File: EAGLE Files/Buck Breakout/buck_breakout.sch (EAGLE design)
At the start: 14 parts

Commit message: Added linear reg to power board. Layout ver 1.
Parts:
- added C7: 1000pF, chips:CAP0603-CAP
- added C8: 1uF, chips:CAP0603-CAP
- added LED2: (no value), chips:LED0603
- added R5, R6: 1M, chips:RESISTOR0402-S
- added R7: 330, chips:RESISTOR0402-S
- added U$2: MCP1725, intelliDesk:MCP1725
- C3: device chips:CAP1206 -> chips:CAP0603-CAP
- JP1: device SparkFun-Connectors:M03PTH -> SparkFun-Connectors:M04PTH
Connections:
- removed net VOUT: C4.1, C5.1, C6.1, JP1.3, L1.2, R2.2, R4.2, U$1.BD
- new net 3.3V: C8.1, JP1.4, R5.2, R7.1, U$2.VOUT
- new net 3.6V: C4.1, C5.1, C6.1, JP1.3, L1.2, R2.2, R4.2, U$1.BD, U$2.SHDN#, U$2.VIN
- new net N$1: LED2.A, R7.2, U$2.PWRGD
- new net N$5: C7.1, U$2.CDELAY
- new net N$6: R5.1, R6.2, U$2.ADJ
- net GND: now also C7.2, C8.2, LED2.C, R6.1, U$2.GND

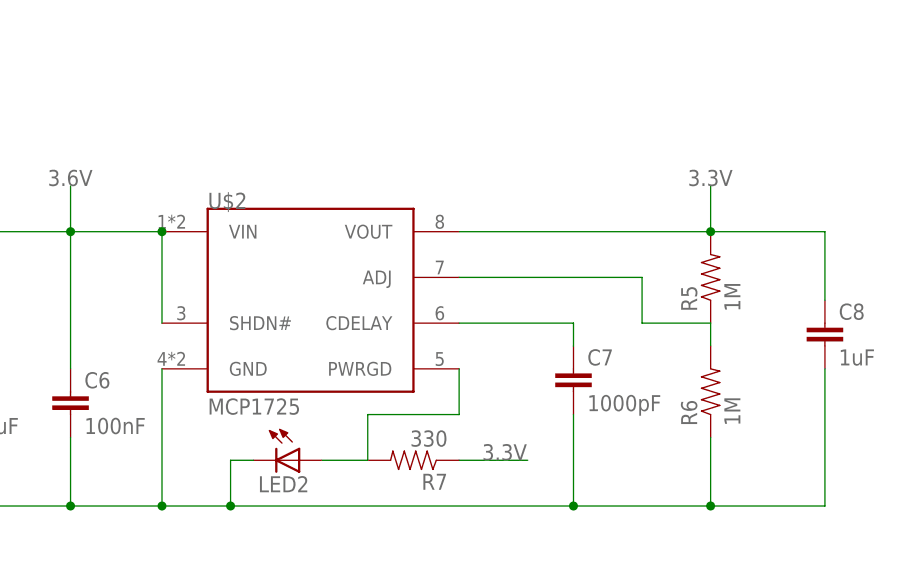
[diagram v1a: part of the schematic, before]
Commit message: Rerouted for nicer layout on linear supply
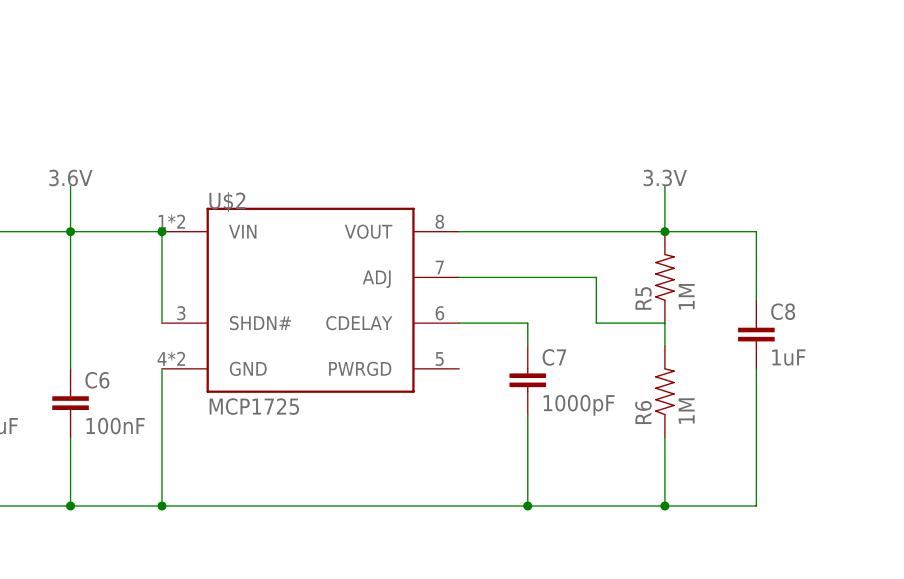
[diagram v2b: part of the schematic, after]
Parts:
- removed LED2: (no value), chips:LED0603
- removed R7: 330, chips:RESISTOR0402-S
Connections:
- removed net N$1: LED2.A, R7.2, U$2.PWRGD
- net 3.3V: no longer R7.1
- net GND: no longer LED2.C
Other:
- moved on the sheet: C7, C8, R5, R6
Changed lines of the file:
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@@
 <part name="R5" library="chips" deviceset="RESISTOR" device="0402-S" value="1M"/>
 <part name="R6" library="chips" deviceset="RESISTOR" device="0402-S" value="1M"/>
-<part name="R7" library="chips" deviceset="RESISTOR" device="0402-S" value="330"/>
-<part name="LED2" library="chips" deviceset="LED" device="0603"/>
 <part name="C7" library="chips" deviceset="CAP" device="0603-CAP" value="1000pF"/>
 <part name="C8" library="chips" deviceset="CAP" device="0603-CAP" value="1uF"/>
@@
 <instance part="GND2" gate="1" x="119.38" y="91.44"/>
 <instance part="U$2" gate="G$1" x="154.94" y="50.8"/>
-<instance part="R5" gate="G$1" x="198.12" y="53.34" rot="R90"/>
-<instance part="R6" gate="G$1" x="198.12" y="40.64" rot="R90"/>
-<instance part="R7" gate="G$1" x="165.1" y="33.02" rot="R180"/>
-<instance part="LED2" gate="G$1" x="152.4" y="33.02" rot="R270"/>
-<instance part="C7" gate="G$1" x="182.88" y="40.64"/>
-<instance part="C8" gate="G$1" x="210.82" y="45.72"/>
+<instance part="R5" gate="G$1" x="193.04" y="53.34" rot="R90"/>
+<instance part="R6" gate="G$1" x="193.04" y="40.64" rot="R90"/>
+<instance part="C7" gate="G$1" x="177.8" y="40.64"/>
+<instance part="C8" gate="G$1" x="203.2" y="45.72"/>
 </instances>
 <busses>
@@
 <pinref part="C7" gate="G$1" pin="2"/>
 <wire x1="127" y1="27.94" x2="114.3" y2="27.94" width="0.1524" layer="91"/>
-<wire x1="137.16" y1="27.94" x2="144.78" y2="27.94" width="0.1524" layer="91"/>
-<wire x1="144.78" y1="27.94" x2="182.88" y2="27.94" width="0.1524" layer="91"/>
-<wire x1="182.88" y1="27.94" x2="182.88" y2="38.1" width="0.1524" layer="91"/>
-<pinref part="LED2" gate="G$1" pin="C"/>
-<wire x1="147.32" y1="33.02" x2="144.78" y2="33.02" width="0.1524" layer="91"/>
-<wire x1="144.78" y1="33.02" x2="144.78" y2="27.94" width="0.1524" layer="91"/>
+<wire x1="137.16" y1="27.94" x2="177.8" y2="27.94" width="0.1524" layer="91"/>
+<wire x1="177.8" y1="27.94" x2="177.8" y2="38.1" width="0.1524" layer="91"/>
 <junction x="137.16" y="27.94"/>
-<junction x="144.78" y="27.94"/>
 <pinref part="R6" gate="G$1" pin="1"/>
-<wire x1="182.88" y1="27.94" x2="198.12" y2="27.94" width="0.1524" layer="91"/>
-<wire x1="198.12" y1="27.94" x2="198.12" y2="35.56" width="0.1524" layer="91"/>
-<junction x="182.88" y="27.94"/>
+<wire x1="177.8" y1="27.94" x2="193.04" y2="27.94" width="0.1524" layer="91"/>
+<wire x1="193.04" y1="27.94" x2="193.04" y2="35.56" width="0.1524" layer="91"/>
+<junction x="177.8" y="27.94"/>
 <pinref part="C8" gate="G$1" pin="2"/>
-<wire x1="210.82" y1="43.18" x2="210.82" y2="27.94" width="0.1524" layer="91"/>
-<wire x1="210.82" y1="27.94" x2="198.12" y2="27.94" width="0.1524" layer="91"/>
-<junction x="198.12" y="27.94"/>
+<wire x1="203.2" y1="43.18" x2="203.2" y2="27.94" width="0.1524" layer="91"/>
+<wire x1="203.2" y1="27.94" x2="193.04" y2="27.94" width="0.1524" layer="91"/>
+<junction x="193.04" y="27.94"/>
 <pinref part="C6" gate="G$1" pin="2"/>
 <wire x1="127" y1="35.56" x2="127" y2="27.94" width="0.1524" layer="91"/>
@@
 <pinref part="U$2" gate="G$1" pin="CDELAY"/>
 <pinref part="C7" gate="G$1" pin="1"/>
-<wire x1="170.18" y1="48.26" x2="182.88" y2="48.26" width="0.1524" layer="91"/>
-<wire x1="182.88" y1="48.26" x2="182.88" y2="45.72" width="0.1524" layer="91"/>
+<wire x1="170.18" y1="48.26" x2="177.8" y2="48.26" width="0.1524" layer="91"/>
+<wire x1="177.8" y1="48.26" x2="177.8" y2="45.72" width="0.1524" layer="91"/>
 </segment>
 </net>
@@
 <pinref part="R6" gate="G$1" pin="2"/>
 <pinref part="R5" gate="G$1" pin="1"/>
-<wire x1="198.12" y1="45.72" x2="198.12" y2="48.26" width="0.1524" layer="91"/>
-<wire x1="198.12" y1="48.26" x2="190.5" y2="48.26" width="0.1524" layer="91"/>
-<wire x1="190.5" y1="48.26" x2="190.5" y2="53.34" width="0.1524" layer="91"/>
+<wire x1="193.04" y1="45.72" x2="193.04" y2="48.26" width="0.1524" layer="91"/>
+<wire x1="193.04" y1="48.26" x2="185.42" y2="48.26" width="0.1524" layer="91"/>
+<wire x1="185.42" y1="48.26" x2="185.42" y2="53.34" width="0.1524" layer="91"/>
 <pinref part="U$2" gate="G$1" pin="ADJ"/>
-<wire x1="190.5" y1="53.34" x2="170.18" y2="53.34" width="0.1524" layer="91"/>
-</segment>
-</net>
-<net name="N$1" class="0">
-<segment>
-<pinref part="U$2" gate="G$1" pin="PWRGD"/>
-<wire x1="170.18" y1="43.18" x2="170.18" y2="38.1" width="0.1524" layer="91"/>
-<pinref part="R7" gate="G$1" pin="2"/>
-<wire x1="170.18" y1="38.1" x2="160.02" y2="38.1" width="0.1524" layer="91"/>
-<wire x1="160.02" y1="38.1" x2="160.02" y2="33.02" width="0.1524" layer="91"/>
-<pinref part="LED2" gate="G$1" pin="A"/>
-<wire x1="160.02" y1="33.02" x2="154.94" y2="33.02" width="0.1524" layer="91"/>
+<wire x1="185.42" y1="53.34" x2="170.18" y2="53.34" width="0.1524" layer="91"/>
 </segment>
 </net>
 <net name="3.3V" class="0">
 <segment>
-<pinref part="R7" gate="G$1" pin="1"/>
-<wire x1="170.18" y1="33.02" x2="177.8" y2="33.02" width="0.1524" layer="91"/>
-<label x="172.72" y="33.02" size="1.778" layer="95"/>
-</segment>
-<segment>
 <pinref part="U$2" gate="G$1" pin="VOUT"/>
-<wire x1="170.18" y1="58.42" x2="198.12" y2="58.42" width="0.1524" layer="91"/>
+<wire x1="170.18" y1="58.42" x2="193.04" y2="58.42" width="0.1524" layer="91"/>
 <pinref part="R5" gate="G$1" pin="2"/>
-<wire x1="198.12" y1="58.42" x2="210.82" y2="58.42" width="0.1524" layer="91"/>
-<junction x="198.12" y="58.42"/>
+<wire x1="193.04" y1="58.42" x2="203.2" y2="58.42" width="0.1524" layer="91"/>
+<junction x="193.04" y="58.42"/>
 <pinref part="C8" gate="G$1" pin="1"/>
-<wire x1="210.82" y1="58.42" x2="210.82" y2="50.8" width="0.1524" layer="91"/>
-<wire x1="198.12" y1="58.42" x2="198.12" y2="63.5" width="0.1524" layer="91"/>
-<label x="195.58" y="63.5" size="1.778" layer="95"/>
-</segment>
-<segment>
+<wire x1="203.2" y1="58.42" x2="203.2" y2="50.8" width="0.1524" layer="91"/>
+<wire x1="193.04" y1="58.42" x2="193.04" y2="63.5" width="0.1524" layer="91"/>
+<label x="190.5" y="63.5" size="1.778" layer="95"/>
+</segment>
+<segment>

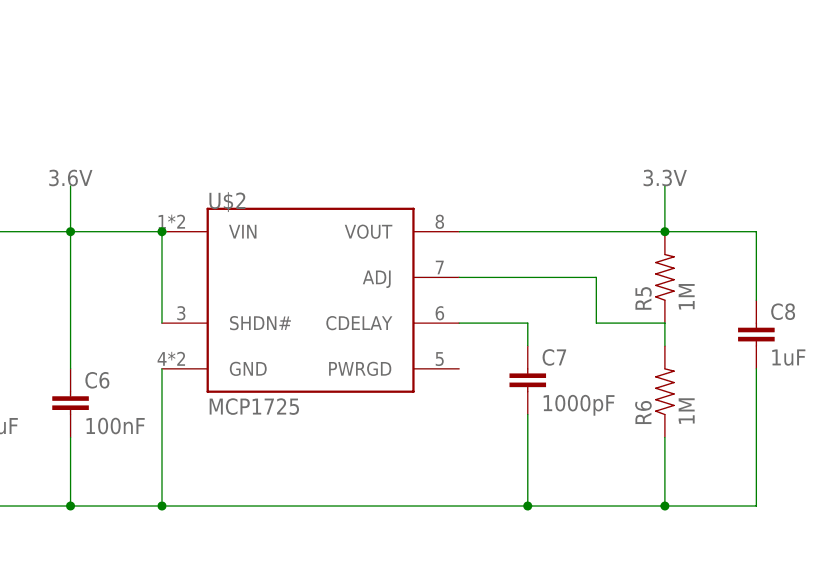
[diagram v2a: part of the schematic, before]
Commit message: fixed via size and removed most silkscreen on power breakout pcb
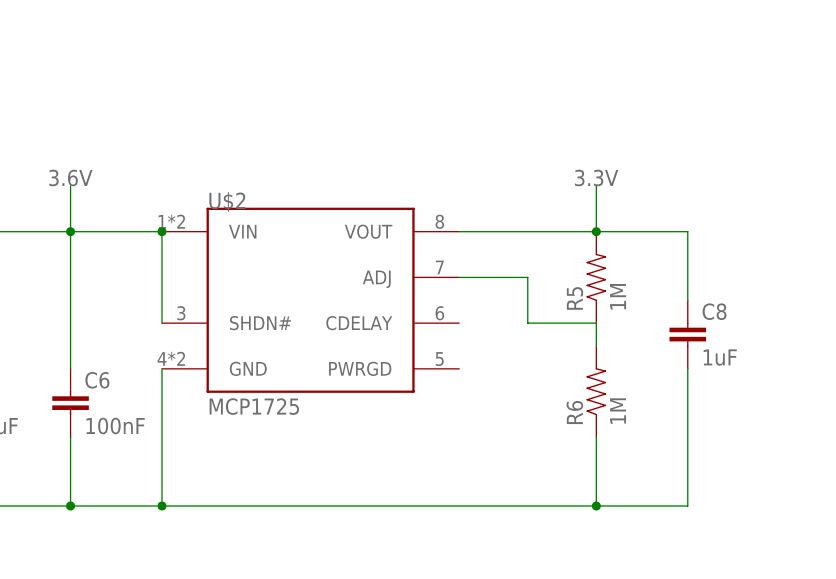
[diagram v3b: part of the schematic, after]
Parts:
- removed C7: 1000pF, chips:CAP0603-CAP
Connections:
- removed net N$5: C7.1, U$2.CDELAY
- net GND: no longer C7.2
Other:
- moved on the sheet: C8, R5, R6
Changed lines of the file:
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@@
 <part name="R5" library="chips" deviceset="RESISTOR" device="0402-S" value="1M"/>
 <part name="R6" library="chips" deviceset="RESISTOR" device="0402-S" value="1M"/>
-<part name="C7" library="chips" deviceset="CAP" device="0603-CAP" value="1000pF"/>
 <part name="C8" library="chips" deviceset="CAP" device="0603-CAP" value="1uF"/>
 </parts>
@@
 <instance part="GND2" gate="1" x="119.38" y="91.44"/>
 <instance part="U$2" gate="G$1" x="154.94" y="50.8"/>
-<instance part="R5" gate="G$1" x="193.04" y="53.34" rot="R90"/>
-<instance part="R6" gate="G$1" x="193.04" y="40.64" rot="R90"/>
-<instance part="C7" gate="G$1" x="177.8" y="40.64"/>
-<instance part="C8" gate="G$1" x="203.2" y="45.72"/>
+<instance part="R5" gate="G$1" x="185.42" y="53.34" rot="R90"/>
+<instance part="R6" gate="G$1" x="185.42" y="40.64" rot="R90"/>
+<instance part="C8" gate="G$1" x="195.58" y="45.72"/>
 </instances>
 <busses>
@@
 <wire x1="137.16" y1="27.94" x2="127" y2="27.94" width="0.1524" layer="91"/>
 <junction x="114.3" y="27.94"/>
-<pinref part="C7" gate="G$1" pin="2"/>
 <wire x1="127" y1="27.94" x2="114.3" y2="27.94" width="0.1524" layer="91"/>
-<wire x1="137.16" y1="27.94" x2="177.8" y2="27.94" width="0.1524" layer="91"/>
-<wire x1="177.8" y1="27.94" x2="177.8" y2="38.1" width="0.1524" layer="91"/>
+<wire x1="137.16" y1="27.94" x2="185.42" y2="27.94" width="0.1524" layer="91"/>
 <junction x="137.16" y="27.94"/>
 <pinref part="R6" gate="G$1" pin="1"/>
-<wire x1="177.8" y1="27.94" x2="193.04" y2="27.94" width="0.1524" layer="91"/>
-<wire x1="193.04" y1="27.94" x2="193.04" y2="35.56" width="0.1524" layer="91"/>
-<junction x="177.8" y="27.94"/>
+<wire x1="185.42" y1="27.94" x2="185.42" y2="35.56" width="0.1524" layer="91"/>
 <pinref part="C8" gate="G$1" pin="2"/>
-<wire x1="203.2" y1="43.18" x2="203.2" y2="27.94" width="0.1524" layer="91"/>
-<wire x1="203.2" y1="27.94" x2="193.04" y2="27.94" width="0.1524" layer="91"/>
-<junction x="193.04" y="27.94"/>
+<wire x1="195.58" y1="43.18" x2="195.58" y2="27.94" width="0.1524" layer="91"/>
+<wire x1="195.58" y1="27.94" x2="185.42" y2="27.94" width="0.1524" layer="91"/>
+<junction x="185.42" y="27.94"/>
 <pinref part="C6" gate="G$1" pin="2"/>
 <wire x1="127" y1="35.56" x2="127" y2="27.94" width="0.1524" layer="91"/>
@@
 </segment>
 </net>
-<net name="N$5" class="0">
-<segment>
-<pinref part="U$2" gate="G$1" pin="CDELAY"/>
-<pinref part="C7" gate="G$1" pin="1"/>
-<wire x1="170.18" y1="48.26" x2="177.8" y2="48.26" width="0.1524" layer="91"/>
-<wire x1="177.8" y1="48.26" x2="177.8" y2="45.72" width="0.1524" layer="91"/>
-</segment>
-</net>
 <net name="N$6" class="0">
 <segment>
 <pinref part="R6" gate="G$1" pin="2"/>
 <pinref part="R5" gate="G$1" pin="1"/>
-<wire x1="193.04" y1="45.72" x2="193.04" y2="48.26" width="0.1524" layer="91"/>
-<wire x1="193.04" y1="48.26" x2="185.42" y2="48.26" width="0.1524" layer="91"/>
-<wire x1="185.42" y1="48.26" x2="185.42" y2="53.34" width="0.1524" layer="91"/>
+<wire x1="185.42" y1="45.72" x2="185.42" y2="48.26" width="0.1524" layer="91"/>
+<wire x1="185.42" y1="48.26" x2="177.8" y2="48.26" width="0.1524" layer="91"/>
+<wire x1="177.8" y1="48.26" x2="177.8" y2="53.34" width="0.1524" layer="91"/>
 <pinref part="U$2" gate="G$1" pin="ADJ"/>
-<wire x1="185.42" y1="53.34" x2="170.18" y2="53.34" width="0.1524" layer="91"/>
+<wire x1="177.8" y1="53.34" x2="170.18" y2="53.34" width="0.1524" layer="91"/>
 </segment>
 </net>
@@
 <segment>
 <pinref part="U$2" gate="G$1" pin="VOUT"/>
-<wire x1="170.18" y1="58.42" x2="193.04" y2="58.42" width="0.1524" layer="91"/>
+<wire x1="170.18" y1="58.42" x2="185.42" y2="58.42" width="0.1524" layer="91"/>
 <pinref part="R5" gate="G$1" pin="2"/>
-<wire x1="193.04" y1="58.42" x2="203.2" y2="58.42" width="0.1524" layer="91"/>
-<junction x="193.04" y="58.42"/>
+<wire x1="185.42" y1="58.42" x2="195.58" y2="58.42" width="0.1524" layer="91"/>
+<junction x="185.42" y="58.42"/>
 <pinref part="C8" gate="G$1" pin="1"/>
-<wire x1="203.2" y1="58.42" x2="203.2" y2="50.8" width="0.1524" layer="91"/>
-<wire x1="193.04" y1="58.42" x2="193.04" y2="63.5" width="0.1524" layer="91"/>
-<label x="190.5" y="63.5" size="1.778" layer="95"/>
-</segment>
-<segment>
+<wire x1="195.58" y1="58.42" x2="195.58" y2="50.8" width="0.1524" layer="91"/>
+<wire x1="185.42" y1="58.42" x2="185.42" y2="63.5" width="0.1524" layer="91"/>
+<label x="182.88" y="63.5" size="1.778" layer="95"/>
+</segment>
+<segment>

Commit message: Added OLED breakout board. (not yet designed) Added linear regulator datasheet. Updated parts library.
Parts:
- R5: value 1M -> 1.1M
- R6: value 1M -> 160k
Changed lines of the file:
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@@
 <part name="GND2" library="supply1" deviceset="GND" device=""/>
 <part name="U$2" library="intelliDesk" deviceset="MCP1725" device=""/>
-<part name="R5" library="chips" deviceset="RESISTOR" device="0402-S" value="1M"/>
-<part name="R6" library="chips" deviceset="RESISTOR" device="0402-S" value="1M"/>
+<part name="R5" library="chips" deviceset="RESISTOR" device="0402-S" value="1.1M"/>
+<part name="R6" library="chips" deviceset="RESISTOR" device="0402-S" value="160k"/>
 <part name="C8" library="chips" deviceset="CAP" device="0603-CAP" value="1uF"/>
 </parts>
